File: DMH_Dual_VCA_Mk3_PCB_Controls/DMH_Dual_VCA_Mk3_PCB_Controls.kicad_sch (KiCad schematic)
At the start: 58 parts, among them J1 TRS_Jack_6.35mm_Sw, J100 IDC_02x05, J11 Conn_01x06, J12 Conn_01x08, J13 Conn_01x06, J14 Conn_01x06, J15 Conn_01x08, J16 Conn_01x06, J18 Conn_02x03_Odd_Even, J19 Conn_02x03_Odd_Even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

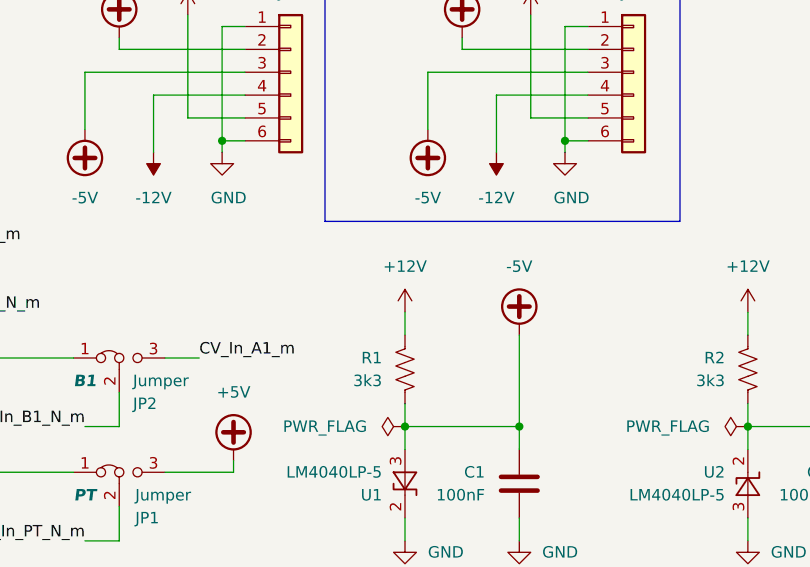
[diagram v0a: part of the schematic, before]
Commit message: Fixed -5V supply circuit mistake
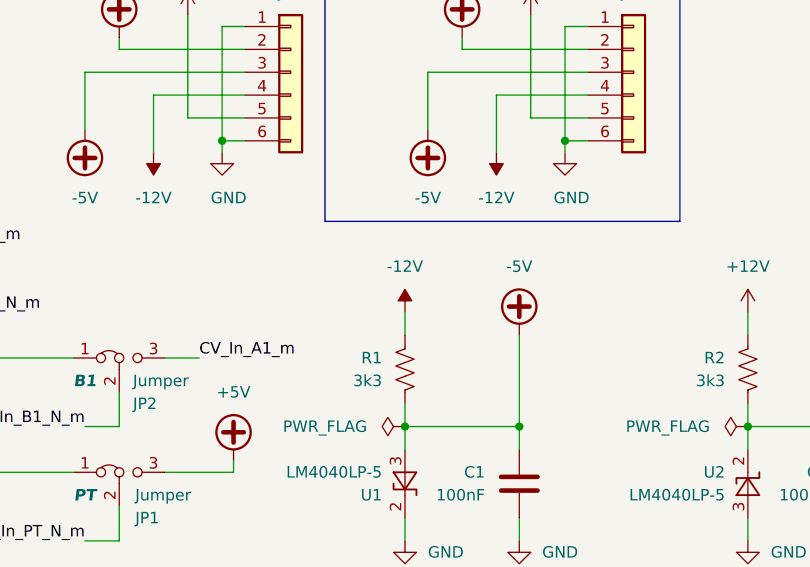
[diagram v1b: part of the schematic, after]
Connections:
- net +12V: no longer R1.2
- net -12V: now also R1.2
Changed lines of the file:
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@@
 	)
 	(symbol
-		(lib_id "power:+12V")
-		(at 114.3 254 0)
-		(unit 1)
-		(body_style 1)
-		(exclude_from_sim no)
-		(in_bom yes)
-		(on_board no)
-		(in_pos_files yes)
-		(dnp no)
-		(fields_autoplaced yes)
-		(property "Reference" "#PWR017"
-			(at 114.3 257.81 0)
-			(hide yes)
-			(show_name no)
-			(do_not_autoplace no)
-			(effects
-				(font
-					(size 1.27 1.27)
-				)
-			)
-		)
-		(property "Value" "+12V"
-			(at 114.3 248.92 0)
-			(show_name no)
-			(do_not_autoplace no)
-			(effects
-				(font
-					(size 1.27 1.27)
-				)
-			)
-		)
-		(property "Footprint" ""
-			(at 114.3 254 0)
-			(hide yes)
-			(show_name no)
-			(do_not_autoplace no)
-			(effects
-				(font
-					(size 1.27 1.27)
-				)
-			)
-		)
-		(property "Datasheet" ""
-			(at 114.3 254 0)
-			(hide yes)
-			(show_name no)
-			(do_not_autoplace no)
-			(effects
-				(font
-					(size 1.27 1.27)
-				)
-			)
-		)
-		(property "Description" "Power symbol creates a global label with name \"+12V\""
-			(at 114.3 254 0)
-			(hide yes)
-			(show_name no)
-			(do_not_autoplace no)
-			(effects
-				(font
-					(size 1.27 1.27)
-				)
-			)
-		)
-		(pin "1"
-		)
-		(instances
-			(project "DMH_Dual_VCA_Mk3_PCB_Controls"
-				(path "/58f4306d-5387-4983-bb08-41a2313fd315"
-					(reference "#PWR017")
-					(unit 1)
-				)
-			)
-		)
-	)
-	(symbol
 		(lib_id "power:+VDC")
 		(at 95.25 270.51 0)
@@
 				)
 			)
+		)
+	)
+	(symbol
+		(lib_id "power:-12V")
+		(at 114.3 254 0)
+		(unit 1)
+		(body_style 1)
+		(exclude_from_sim no)
+		(in_bom yes)
+		(on_board no)
+		(in_pos_files yes)
+		(dnp no)
+		(fields_autoplaced yes)
+		(property "Reference" "#PWR017"
+			(at 114.3 257.81 0)
+			(hide yes)
+			(show_name no)
+			(do_not_autoplace no)
+			(effects
+				(font
+					(size 1.27 1.27)
+				)
+			)
+		)
+		(property "Value" "-12V"
+			(at 114.3 248.92 0)
+			(show_name no)
+			(do_not_autoplace no)
+			(effects
+				(font
+					(size 1.27 1.27)
+				)
+			)
+		)
+		(property "Footprint" ""
+			(at 114.3 254 0)
+			(hide yes)
+			(show_name no)
+			(do_not_autoplace no)
+			(effects
+				(font
+					(size 1.27 1.27)
+				)
+			)
+		)
+		(property "Datasheet" ""
+			(at 114.3 254 0)
+			(hide yes)
+			(show_name no)
+			(do_not_autoplace no)
+			(effects
+				(font
+					(size 1.27 1.27)
+				)
+			)
+		)
+		(property "Description" "Power symbol creates a global label with name \"-12V\""
+			(at 114.3 254 0)
+			(hide yes)
+			(show_name no)
+			(do_not_autoplace no)
+			(effects
+				(font
+					(size 1.27 1.27)
+				)
+			)
+		)
+		(pin "1"
+		)
+		(instances
+			(project "DMH_Dual_VCA_Mk3_PCB_Controls"
+				(path "/58f4306d-5387-4983-bb08-41a2313fd315"
+					(reference "#PWR017")
+					(unit 1)
+				)
+			)

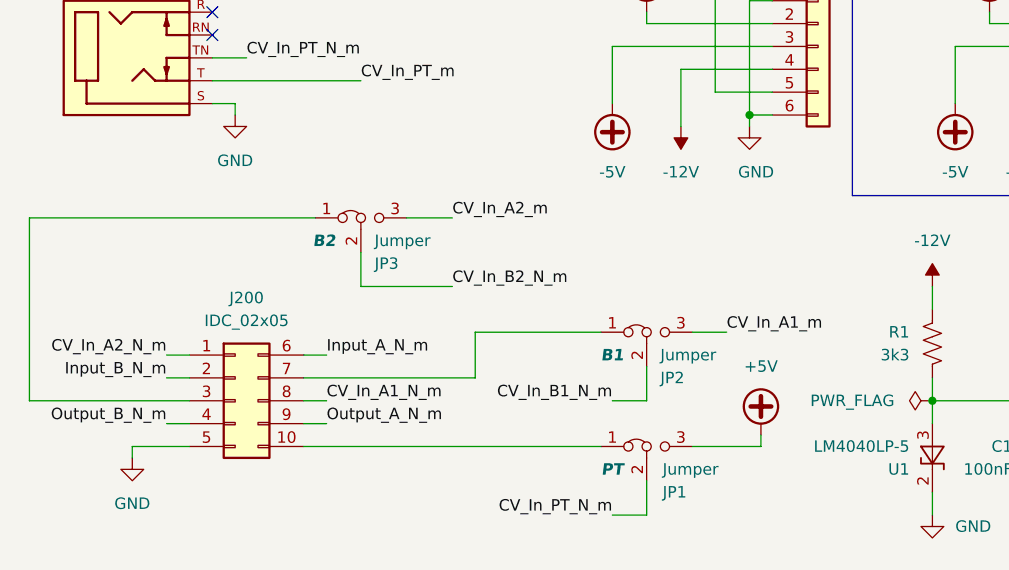
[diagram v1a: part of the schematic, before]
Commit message: Added jumper to normalize Input B to A
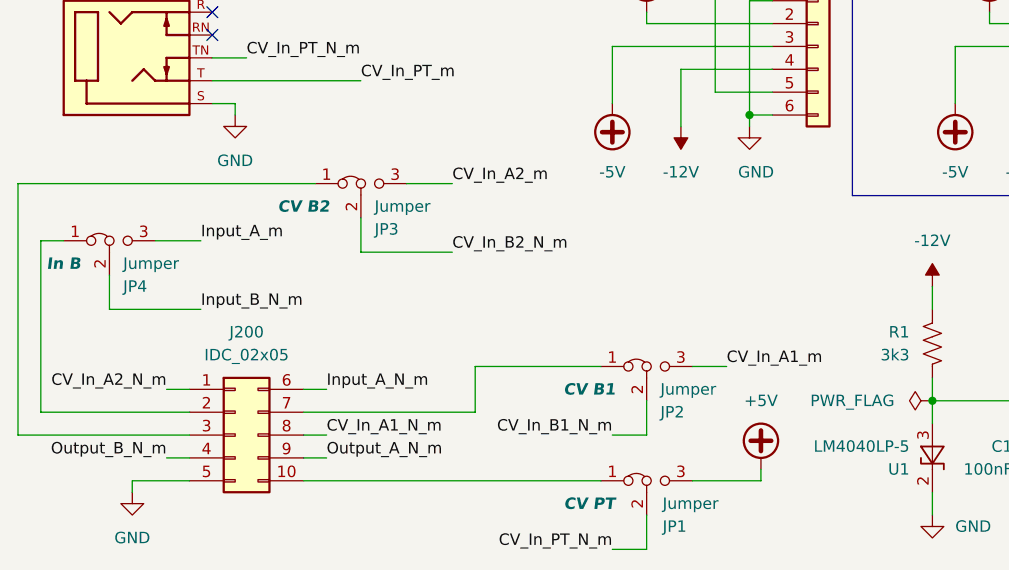
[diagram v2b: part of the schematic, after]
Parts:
- added JP4: Jumper, Connector_PinHeader_2.54mm:PinHeader_1x03_P2.54mm_Vertical, symbol Jumper:Jumper_3_Bridged12
- JP1: Function PT -> CV PT
- JP2: Function B1 -> CV B1
- JP3: Function B2 -> CV B2
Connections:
- net Input_A_m: now also JP4.3 (B)
- net Input_B_N_m: now also JP4.2 (C); no longer J200.2 (Pin_2)
- new net: J200.2 (Pin_2), JP4.1 (A)
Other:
- moved on the sheet: J200, JP1, JP2, JP3

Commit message: Main PCB routing in progress
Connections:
- net Output_A_N_m: now also J200.4 (Pin_4); no longer J200.9 (Pin_9)
- net Output_B_N_m: now also J200.9 (Pin_9); no longer J200.4 (Pin_4)
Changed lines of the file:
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@@
 	)
 	(label "Output_A_N_m"
-		(at 46.99 273.05 0)
-		(effects
-			(font
-				(size 1.27 1.27)
-			)
-			(justify left bottom)
+		(at 29.21 273.05 180)
+		(effects
+			(font
+				(size 1.27 1.27)
+			)
+			(justify right bottom)
 		)
 	)
@@
 	)
 	(label "Output_B_N_m"
-		(at 29.21 273.05 180)
-		(effects
-			(font
-				(size 1.27 1.27)
-			)
-			(justify right bottom)
-		)
-	)
+		(at 46.99 273.05 0)
+		(effects
+			(font
+				(size 1.27 1.27)
+			)
+			(justify left bottom)
+		)
+	)

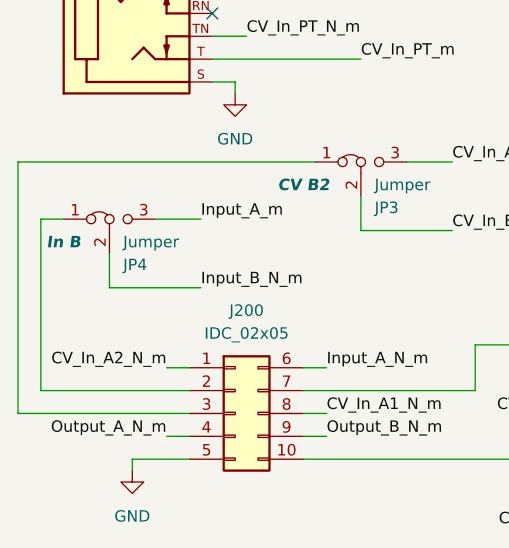
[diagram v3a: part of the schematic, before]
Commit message: Main PCB routing done
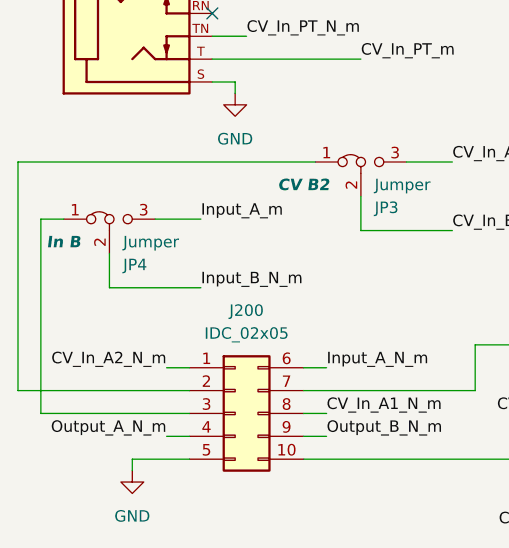
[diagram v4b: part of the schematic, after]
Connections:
- net at J200.2 (Pin_2): now also JP3.1 (A); no longer JP4.1 (A)
- net at J200.3 (Pin_3): now also JP4.1 (A); no longer JP3.1 (A)
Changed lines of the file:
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@@
-	(wire
-		(pts
-			(xy 12.7 270.51) (xy 31.75 270.51)
-		)
-		(stroke
-			(width 0)
-			(type default)
-		)
-	)
 	(wire
 		(pts
@@
 	(wire
 		(pts
-			(xy 12.7 242.57) (xy 12.7 270.51)
+			(xy 12.7 242.57) (xy 12.7 267.97)
 		)
 		(stroke
@@
 	(wire
 		(pts
+			(xy 12.7 267.97) (xy 31.75 267.97)
+		)
+		(stroke
+			(width 0)
+			(type default)
+		)
+	)
+	(wire
+		(pts
 			(xy 314.96 111.76) (xy 317.5 111.76)
 		)
@@
 	(wire
 		(pts
+			(xy 15.24 248.92) (xy 15.24 270.51)
+		)
+		(stroke
+			(width 0)
+			(type default)
+		)
+	)
+	(wire
+		(pts
 			(xy 254 88.9) (xy 266.7 88.9)
 		)
@@
 	(wire
 		(pts
-			(xy 15.24 248.92) (xy 15.24 267.97)
-		)
-		(stroke
-			(width 0)
-			(type default)
-		)
-	)
-	(wire
-		(pts
 			(xy 336.55 152.4) (xy 342.9 152.4)
 		)
@@
 	(wire
 		(pts
+			(xy 15.24 270.51) (xy 31.75 270.51)
+		)
+		(stroke
+			(width 0)
+			(type default)
+		)
+	)
+	(wire
+		(pts
 			(xy 254 264.16) (xy 254 266.7)
 		)
@@
 		)
 		(stroke
-			(width 0)
-			(type default)
-		)
-	)
-	(wire
-		(pts
-			(xy 15.24 267.97) (xy 31.75 267.97)
-		)
-		(stroke
